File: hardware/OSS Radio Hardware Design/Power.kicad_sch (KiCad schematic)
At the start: 5 parts, among them U3 NCP1117-3.3_SOT223

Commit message: working on battery circuitry
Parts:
- added Q2: AO3401A, Package_TO_SOT_SMD:SOT-23, symbol Transistor_FET:AO3401A
- added U2: S-8252AAZ-M6T1U, SOT236-A-PKG_MP006-A-P-SD-2.1_ABL, symbol 2025-04-02_22-14-21:S-8252AAZ-M6T1U
- added U9: MCP73844-840I/MS, MSOP8_MC_MCH, symbol 2025-04-02_22-09-11:MCP73844-840I_MS
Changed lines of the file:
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@@
+	)
+	(symbol
+		(lib_id "2025-04-02_22-09-11:MCP73844-840I_MS")
+		(at 87.63 96.52 0)
+		(unit 1)
+		(exclude_from_sim no)
+		(in_bom yes)
+		(on_board yes)
+		(dnp no)
+		(fields_autoplaced yes)
+		(property "Reference" "U9"
+			(at 120.65 86.36 0)
+			(effects
+				(font
+					(size 1.524 1.524)
+				)
+			)
+		)
+		(property "Value" "MCP73844-840I/MS"
+			(at 120.65 88.9 0)
+			(effects
+				(font
+					(size 1.524 1.524)
+				)
+			)
+		)
+		(property "Footprint" "MSOP8_MC_MCH"
+			(at 87.63 96.52 0)
+			(effects
+				(font
+					(size 1.27 1.27)
+					(italic yes)
+				)
+				(hide yes)
+			)
+		)
+		(property "Datasheet" "MCP73844-840I/MS"
+			(at 87.63 96.52 0)
+			(effects
+				(font
+					(size 1.27 1.27)
+					(italic yes)
+				)
+				(hide yes)
+			)
+		)
+		(property "Description" ""
+			(at 87.63 96.52 0)
+			(effects
+				(font
+					(size 1.27 1.27)
+				)
+				(hide yes)
+			)
+		)
+		(pin "5"
+		)
+		(pin "6"
+		)
+		(pin "1"
+		)
+		(pin "2"
+		)
+		(pin "4"
+		)
+		(pin "8"
+		)
+		(pin "7"
+		)
+		(pin "3"
+		)
+		(instances
+			(project ""
+				(path "/fd5c68a7-f5d0-4135-a258-bde3ebf63307/c701d20d-e266-4c46-aeb3-ff3d813a359d"
+					(reference "U9")
+					(unit 1)
+				)
+			)
+		)
 	)
 	(symbol
@@
 	)
 	(symbol
+		(lib_id "Transistor_FET:AO3401A")
+		(at 123.19 53.34 90)
+		(unit 1)
+		(exclude_from_sim no)
+		(in_bom yes)
+		(on_board yes)
+		(dnp no)
+		(fields_autoplaced yes)
+		(property "Reference" "Q2"
+			(at 123.19 44.45 90)
+			(effects
+				(font
+					(size 1.27 1.27)
+				)
+			)
+		)
+		(property "Value" "AO3401A"
+			(at 123.19 46.99 90)
+			(effects
+				(font
+					(size 1.27 1.27)
+				)
+			)
+		)
+		(property "Footprint" "Package_TO_SOT_SMD:SOT-23"
+			(at 125.095 48.26 0)
+			(effects
+				(font
+					(size 1.27 1.27)
+					(italic yes)
+				)
+				(justify left)
+				(hide yes)
+			)
+		)
+		(property "Datasheet" "http://www.aosmd.com/pdfs/datasheet/AO3401A.pdf"
+			(at 127 48.26 0)
+			(effects
+				(font
+					(size 1.27 1.27)
+				)
+				(justify left)
+				(hide yes)
+			)
+		)
+		(property "Description" "-4.0A Id, -30V Vds, P-Channel MOSFET, SOT-23"
+			(at 123.19 53.34 0)
+			(effects
+				(font
+					(size 1.27 1.27)
+				)
+				(hide yes)
+			)
+		)
+		(pin "3"
+		)
+		(pin "2"
+		)
+		(pin "1"
+		)
+		(instances
+			(project ""
+				(path "/fd5c68a7-f5d0-4135-a258-bde3ebf63307/c701d20d-e266-4c46-aeb3-ff3d813a359d"
+					(reference "Q2")
+					(unit 1)
+				)
+			)
+		)
+	)
+	(symbol
 		(lib_id "power:GND")
 		(at 251.46 50.8 0)
@@
 					(unit 1)
 				)
+			)
+		)
+	)
+	(symbol
+		(lib_id "2025-04-02_22-14-21:S-8252AAZ-M6T1U")
+		(at 184.15 95.25 0)
+		(unit 1)
+		(exclude_from_sim no)
+		(in_bom yes)
+		(on_board yes)
+		(dnp no)
+		(fields_autoplaced yes)
+		(property "Reference" "U2"
+			(at 204.47 82.55 0)
+			(effects
+				(font
+					(size 1.524 1.524)
+				)
+			)
+		)
+		(property "Value" "S-8252AAZ-M6T1U"
+			(at 204.47 85.09 0)
+			(effects
+				(font
+					(size 1.524 1.524)
+				)
+			)
+		)
+		(property "Footprint" "SOT236-A-PKG_MP006-A-P-SD-2.1_ABL"
+			(at 184.15 95.25 0)
+			(effects
+				(font
+					(size 1.27 1.27)
+					(italic yes)
+				)
+				(hide yes)
+			)
+		)
+		(property "Datasheet" "S-8252AAZ-M6T1U"
+			(at 184.15 95.25 0)
+			(effects
+				(font
+					(size 1.27 1.27)
+					(italic yes)
+				)
+				(hide yes)
+			)
+		)
+		(property "Description" ""
+			(at 184.15 95.25 0)
+			(effects
+				(font
+					(size 1.27 1.27)
+				)
+				(hide yes)
+			)
+		)
+		(pin "5"
+		)
+		(pin "3"
+		)
+		(pin "4"
+		)
+		(pin "2"
+		)
+		(pin "6"
+		)
+		(pin "1"
+		)
+		(instances
+			(project ""
+				(path "/fd5c68a7-f5d0-4135-a258-bde3ebf63307/c701d20d-e266-4c46-aeb3-ff3d813a359d"
+					(reference "U2")
+					(unit 1)
+				)

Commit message: BOM consolidation
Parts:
- added C48, C50: 4.7u, symbol Device:C
- C5, C6: value 10u -> 4.7u
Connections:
- net 3V3_MCU: now also C48.2
- net at C5.2, R10.1, R12.1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: now also C50.2
- net at C5.1, C6.1: now also C48.1, C50.1
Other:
- moved on the sheet: C6, R12

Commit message: working on battery protection and charge
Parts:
- added C53, C54: 4.7u, symbol Device:C_Small
- added C55, C56, C57: 100n, symbol Device:C_Small
- added J7: BATT_CONN, symbol Connector:Conn_01x03_Socket
- added Q3, Q4: AO3400A, Package_TO_SOT_SMD:SOT-23, symbol Transistor_FET:AO3400A
- added R25: 0.05, symbol Device:R_Small
- added R26, R29: 100k, symbol Device:R_Small
- added R27: 27k, symbol Device:R_Small
- added R28: 5k1, symbol Device:R_Small
- added R30, R31, R32, R33, R34, R35: 1k, symbol Device:R_Small
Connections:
- net 3V3_MCU: now also R28.2
- net GND: now also U9.6 (VSS), C53.2, C54.2, C55.2, Q4.2 (S), R27.2
- net V_BAT: now also Q2.3 (D), U9.7 (VBAT), C53.1, C54.1, J7.1 (Pin_1), R30.2, R34.1
- net at U9.1 (SENSE): now also Q2.2 (S), R25.2
- net V_CHG: now reaches U9.2 (VDD)
- net V_CHG: now also R25.1, R26.1, R29.2
- net CHGR_STAT: now reaches U9.3 (STAT1)
- net CHGR_STAT: now also R28.1
- net at U9.4 (EN): now also R29.1
- net at U9.5 (TIMER): now also C55.1
- net at U9.8 (DRV): now also Q2.1 (G)
- net at U2.1 (DO): now also Q3.1 (G)
- net at U2.2 (CO): now also Q4.1 (G)
- net at U2.3 (VM): now also R33.2
- net at U2.4 (VC): now also C56.1, C57.2, R31.1, R35.2
- net at U2.5 (VDD): now also C57.1, R30.1, R34.2
- net at U2.6 (VSS): now also C56.2, J7.3 (Pin_3), Q3.2 (S), R32.2
- new net: J7.2 (Pin_2), R31.2, R35.1
- new net: R32.1, R33.1
- new net: Q3.3 (D), Q4.3 (D)
- new net CHGR_CONN: R26.2, R27.1
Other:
- note added: "+"
- note added: "-"
- note added: "9-12V"
- note added: "Battery Charge and Protect"
- moved on the sheet: Q2, U2, U9

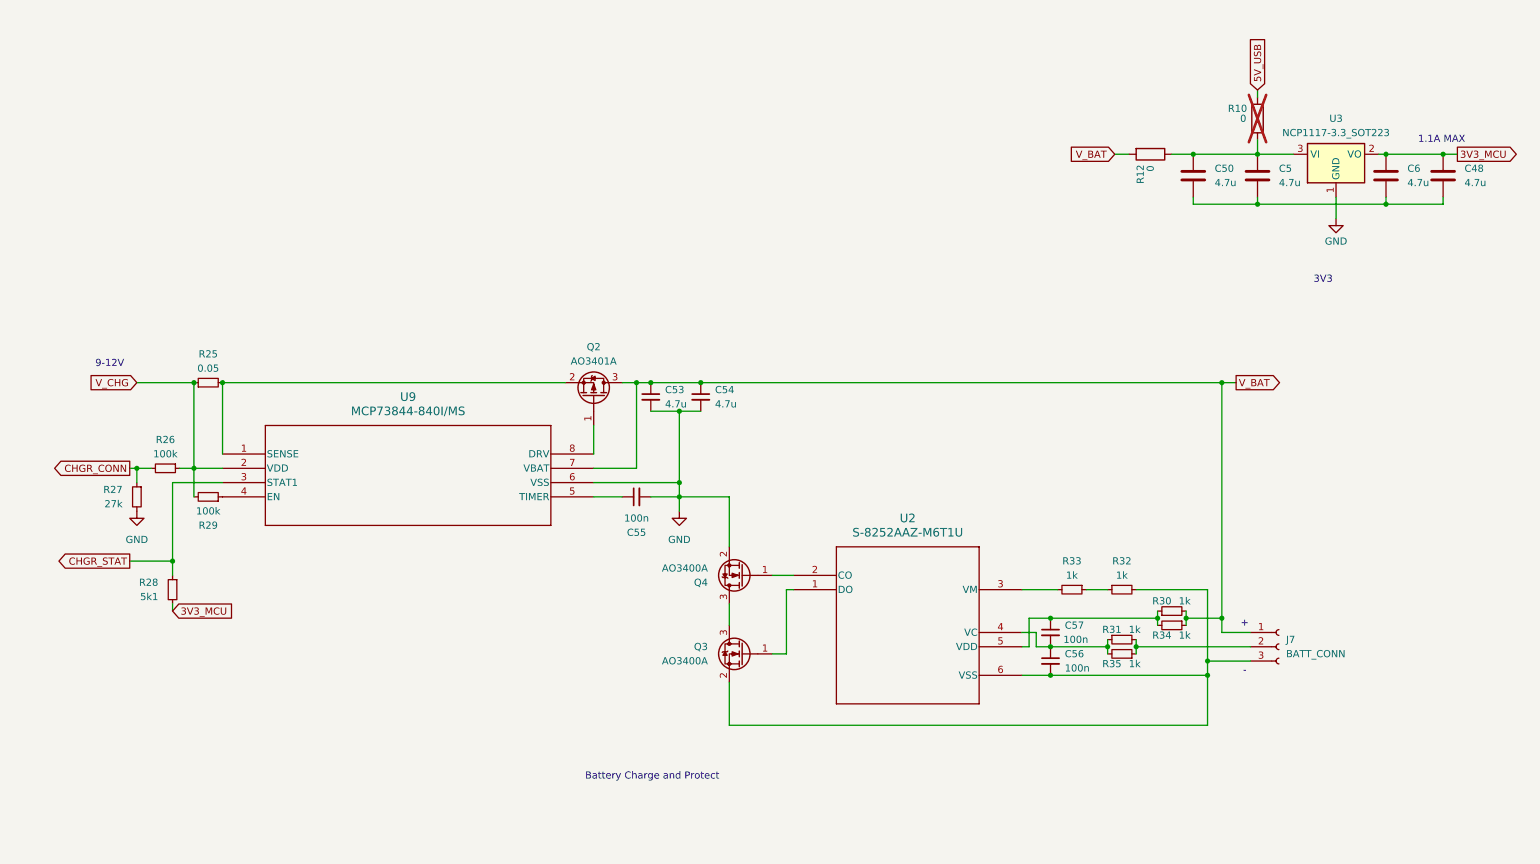
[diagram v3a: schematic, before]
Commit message: finished battery and charger. Now all i need is RF output stages, GPS, and Buttons
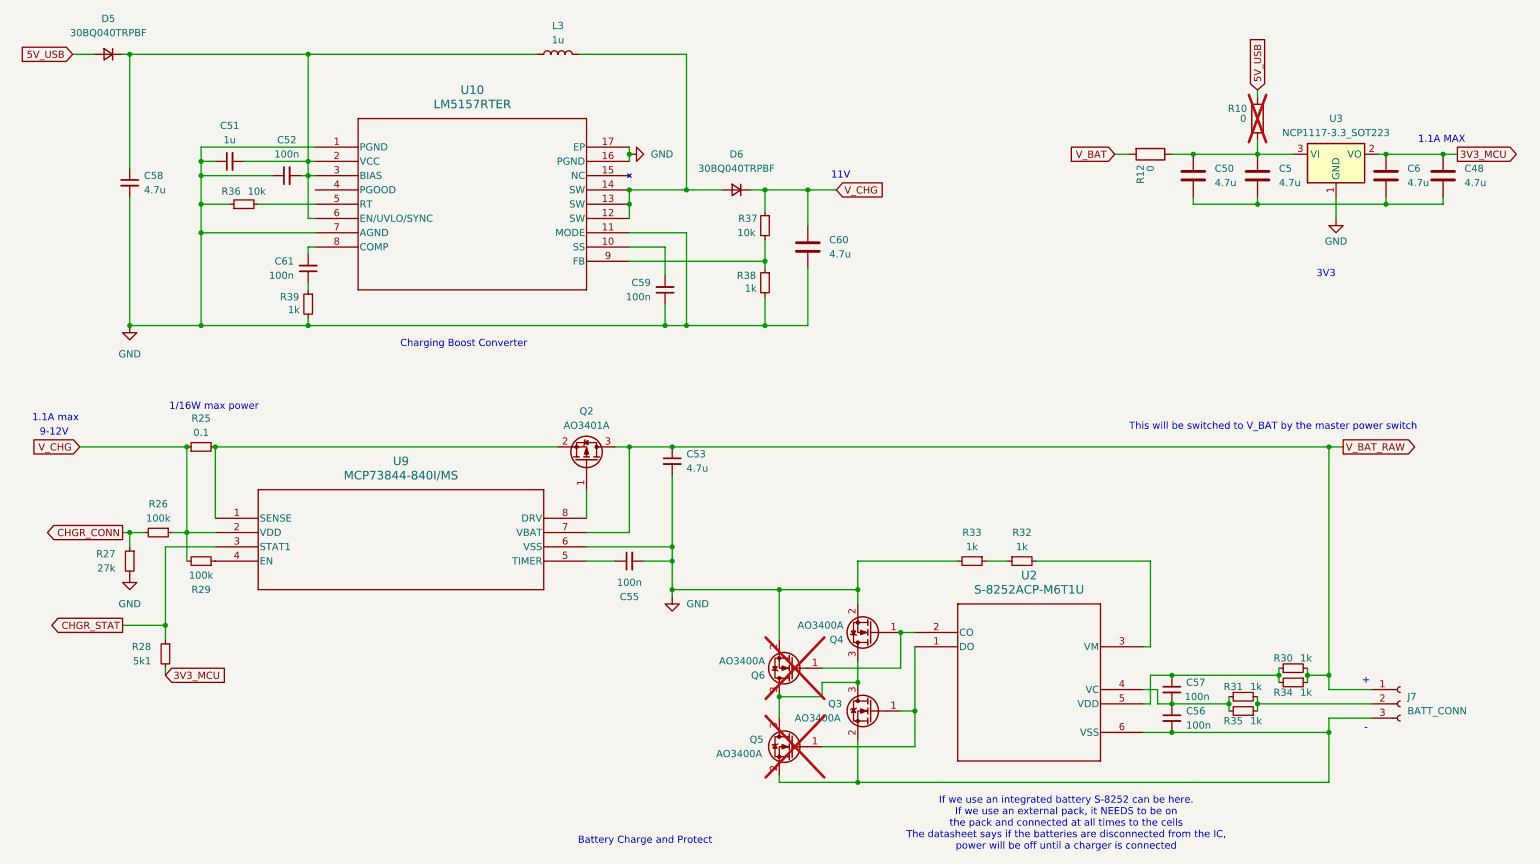
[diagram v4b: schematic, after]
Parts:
- removed C54: 4.7u, symbol Device:C_Small
- added C51: 1u, symbol Device:C_Small
- added C52, C59, C61: 100n, symbol Device:C_Small
- added C58: 4.7u, symbol Device:C_Small
- added C60: 4.7u, symbol Device:C
- added D5, D6: 30BQ040TRPBF, symbol Device:D_Small
- added L3: 1u, symbol Device:L
- added Q5, Q6: AO3400A, Package_TO_SOT_SMD:SOT-23, symbol Transistor_FET:AO3400A
- added R36, R37: 10k, symbol Device:R_Small
- added R38, R39: 1k, symbol Device:R_Small
- added U10: LM5157RTER, QFN_57RTER_TEX, symbol 2025-04-04_20-55-54:LM5157RTER
- R25: value 0.05 -> 0.1
- U2: value S-8252AAZ-M6T1U -> S-8252ACP-M6T1U
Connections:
- net 5V_USB: now also D5.2 (A)
- net GND: now also R33.2, C51.1, C52.1, C58.2, C59.1, C60.1, Q6.2 (S), R36.1, R38.2, R39.2, U10.1 (PGND), U10.11 (MODE), U10.16 (PGND), U10.17 (EP), U10.7 (AGND)
- net V_BAT: no longer C53.1, J7.1 (Pin_1), Q2.3 (D), R30.2, R34.1, U9.7 (VBAT)
- net V_CHG: now also C60.2, D6.1 (K), R37.1
- net at C56.2, J7.3 (Pin_3), Q3.2 (S)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: now also Q5.2 (S); no longer R32.2
- net at U2.3 (VM): now also R32.2; no longer R33.2
- net at Q4.1 (G), U2.2 (CO): now also Q6.1 (G)
- net at Q3.3 (D), Q4.3 (D): now also Q5.3 (D), Q6.3 (D)
- net at Q3.1 (G), U2.1 (DO): now also Q5.1 (G)
- new net: D6.2 (A), L3.2, U10.12 (SW), U10.13 (SW), U10.14 (SW)
- new net: R37.2, R38.1, U10.9 (FB)
- new net: C59.2, U10.10 (SS)
- new net: C51.2, C52.2, C58.1, D5.1 (K), L3.1, U10.2 (VCC), U10.3 (BIAS), U10.6 (EN/UVLO/SYNC)
- new net: R36.2, U10.5 (RT)
- new net: C61.2, U10.8 (COMP)
- new net: C61.1, R39.1
- new net V_BAT_RAW: C53.1, J7.1 (Pin_1), Q2.3 (D), R30.2, R34.1, U9.7 (VBAT)
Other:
- note added: "1.1A max"
- note added: "1/16W max power"
- note added: "11V"
- note added: "Charging Boost Converter"
- note added: "If we use an integrated battery S-8252 can be here. If we use an external pack, it NEEDS to be on the pack and connected at all times to the cells The datasheet says if the batteries are disconnected from the IC, power will be off until a charger is connected"
- note added: "This will be switched to V_BAT by the master power switch"
- moved on the sheet: C53, C55, C56, C57, J7, Q2, Q3, Q4, R25, R26, R27, R28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

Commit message: probably going to change over to PDM for audio out with an opamp
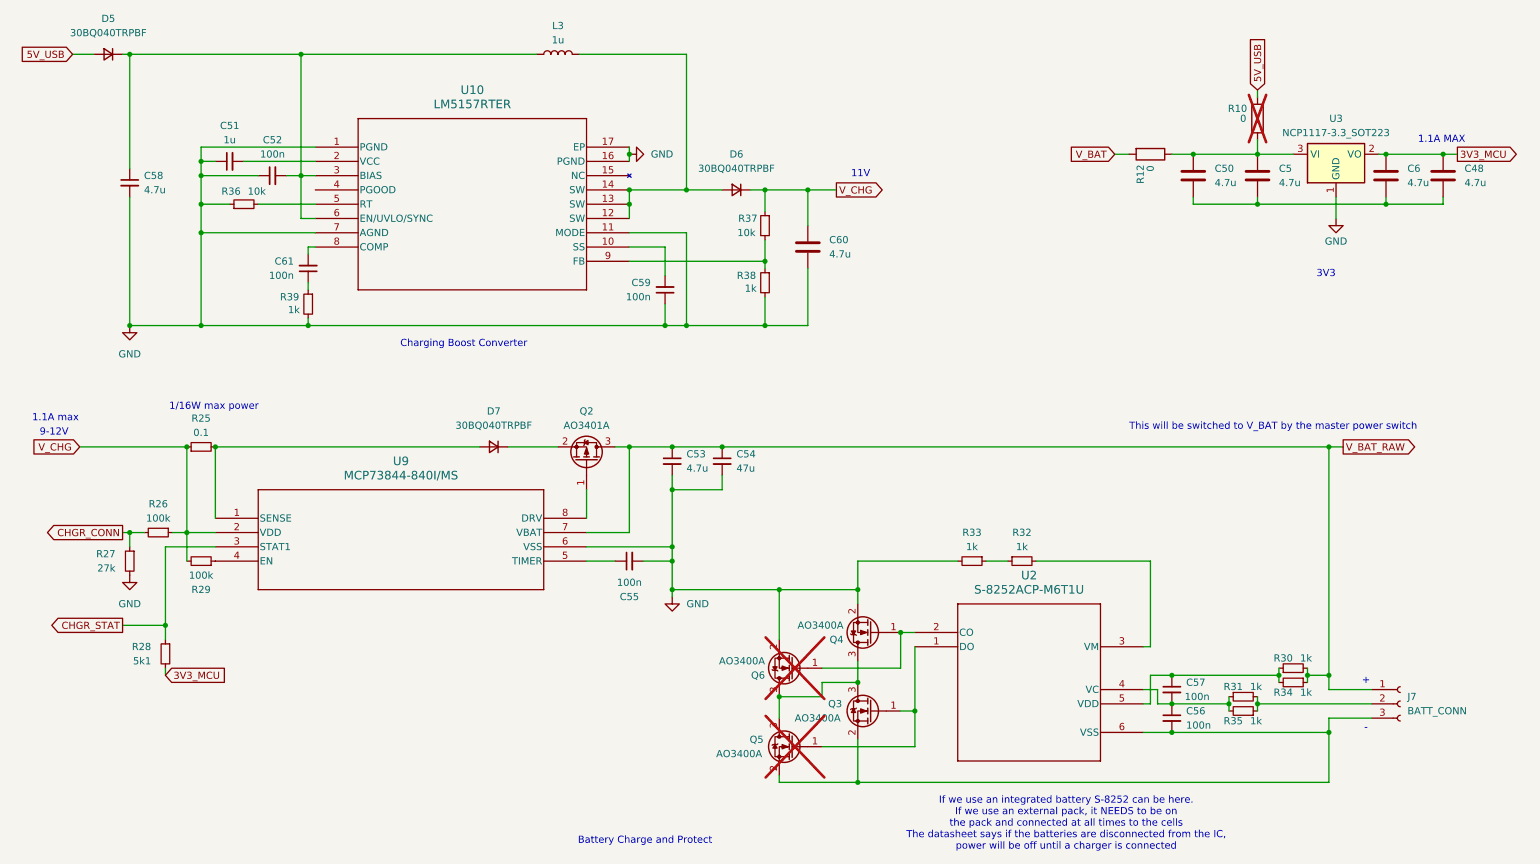
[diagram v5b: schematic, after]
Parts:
- added C54: 47u, symbol Device:C_Small
- added D7: 30BQ040TRPBF, symbol Device:D_Small
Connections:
- net GND: now also C54.2
- net V_BAT_RAW: now also C54.1
- net at R25.2, U9.1 (SENSE): now also D7.2 (A); no longer Q2.2 (S)
- net at C52.2, C58.1, D5.1 (K)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: no longer C51.2, U10.2 (VCC)
- new net: C51.2, U10.2 (VCC)
- new net: D7.1 (K), Q2.2 (S)
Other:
- moved on the sheet: C52

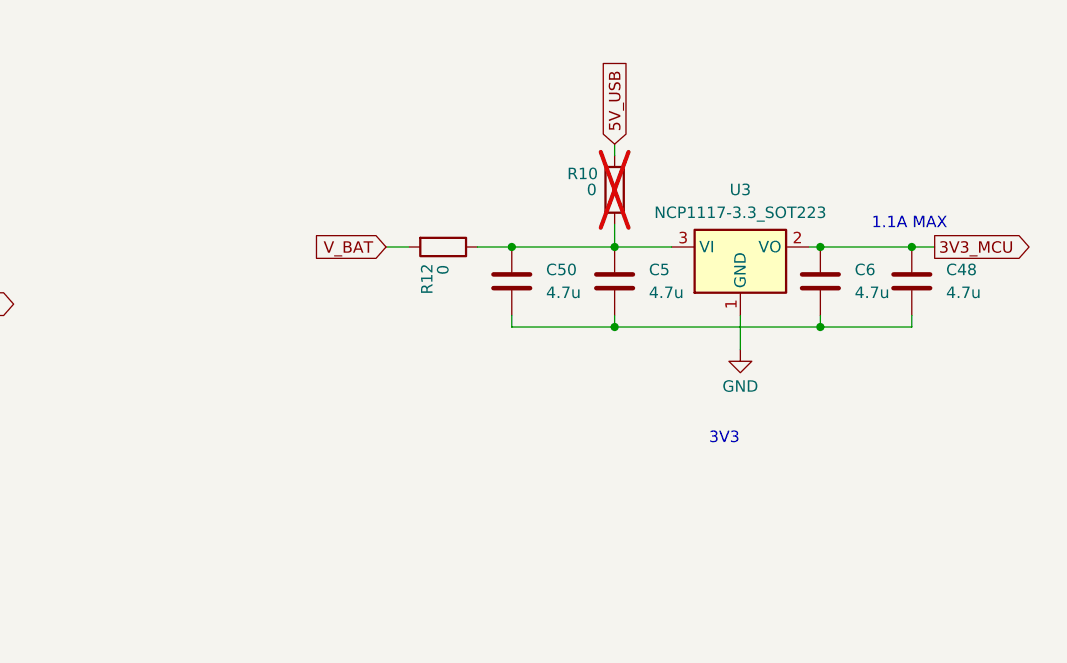
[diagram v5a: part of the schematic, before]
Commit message: added new power supply for audio, working on new audio amp
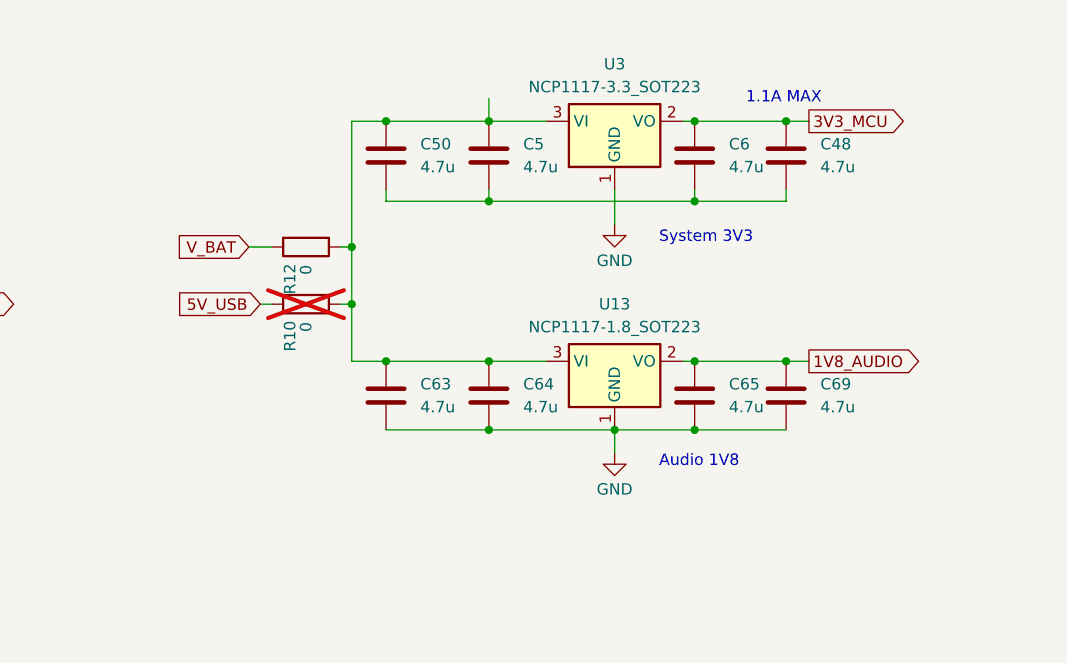
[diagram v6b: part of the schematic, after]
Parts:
- added C63, C64, C65, C69: 4.7u, symbol Device:C
- added U13: NCP1117-1.8_SOT223, Package_TO_SOT_SMD:SOT-223-3_TabPin2, symbol Regulator_Linear:NCP1117-1.8_SOT223
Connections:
- net GND: now also C63.1, C64.1, C65.1, C69.1, U13.1 (GND)
- net at C5.2, C50.2, R10.1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: now also C63.2, C64.2, U13.3 (VI)
- new net 1V8_AUDIO: C65.2, C69.2, U13.2 (VO)
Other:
- note added: "Audio 1V8"
- note added: "System 3V3"
- note removed: "3V3"
- moved on the sheet: C48, C5, C50, C6, R10, R12, U3
